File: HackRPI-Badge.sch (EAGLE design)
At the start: 24 parts, among them IC1 74595, IC2 74595, IC3 74595

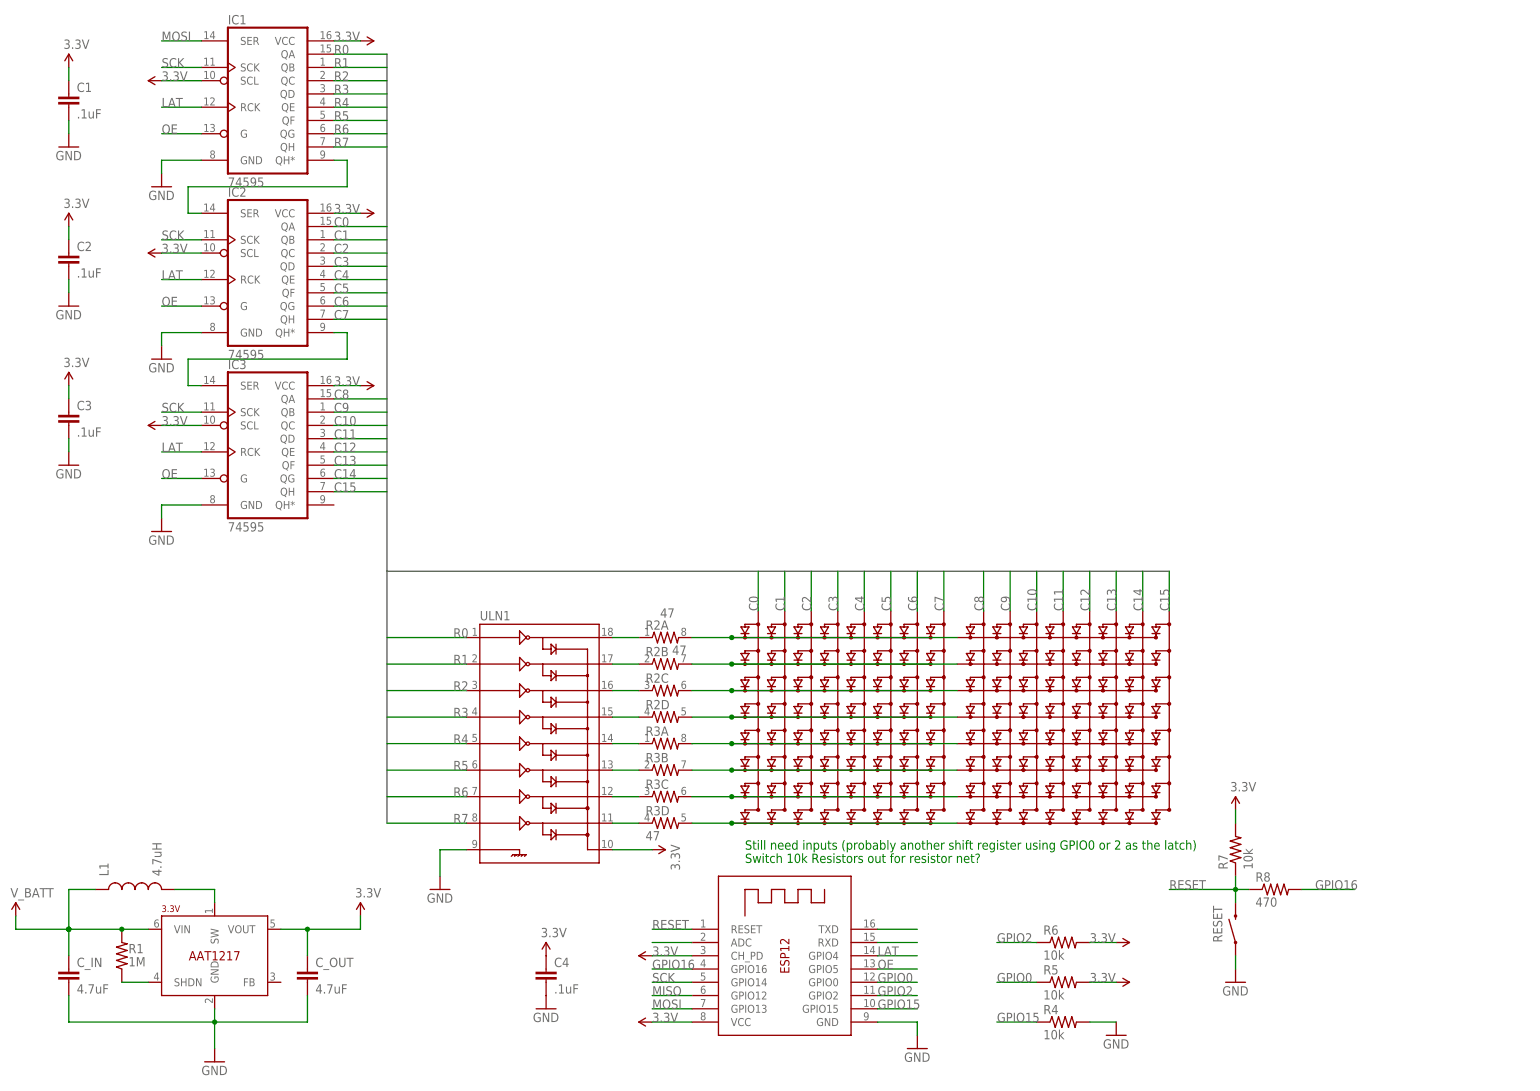
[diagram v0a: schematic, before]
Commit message: Moved resistor nets to ensure constant LED brightness, added serial connector, added 74HC165 for input
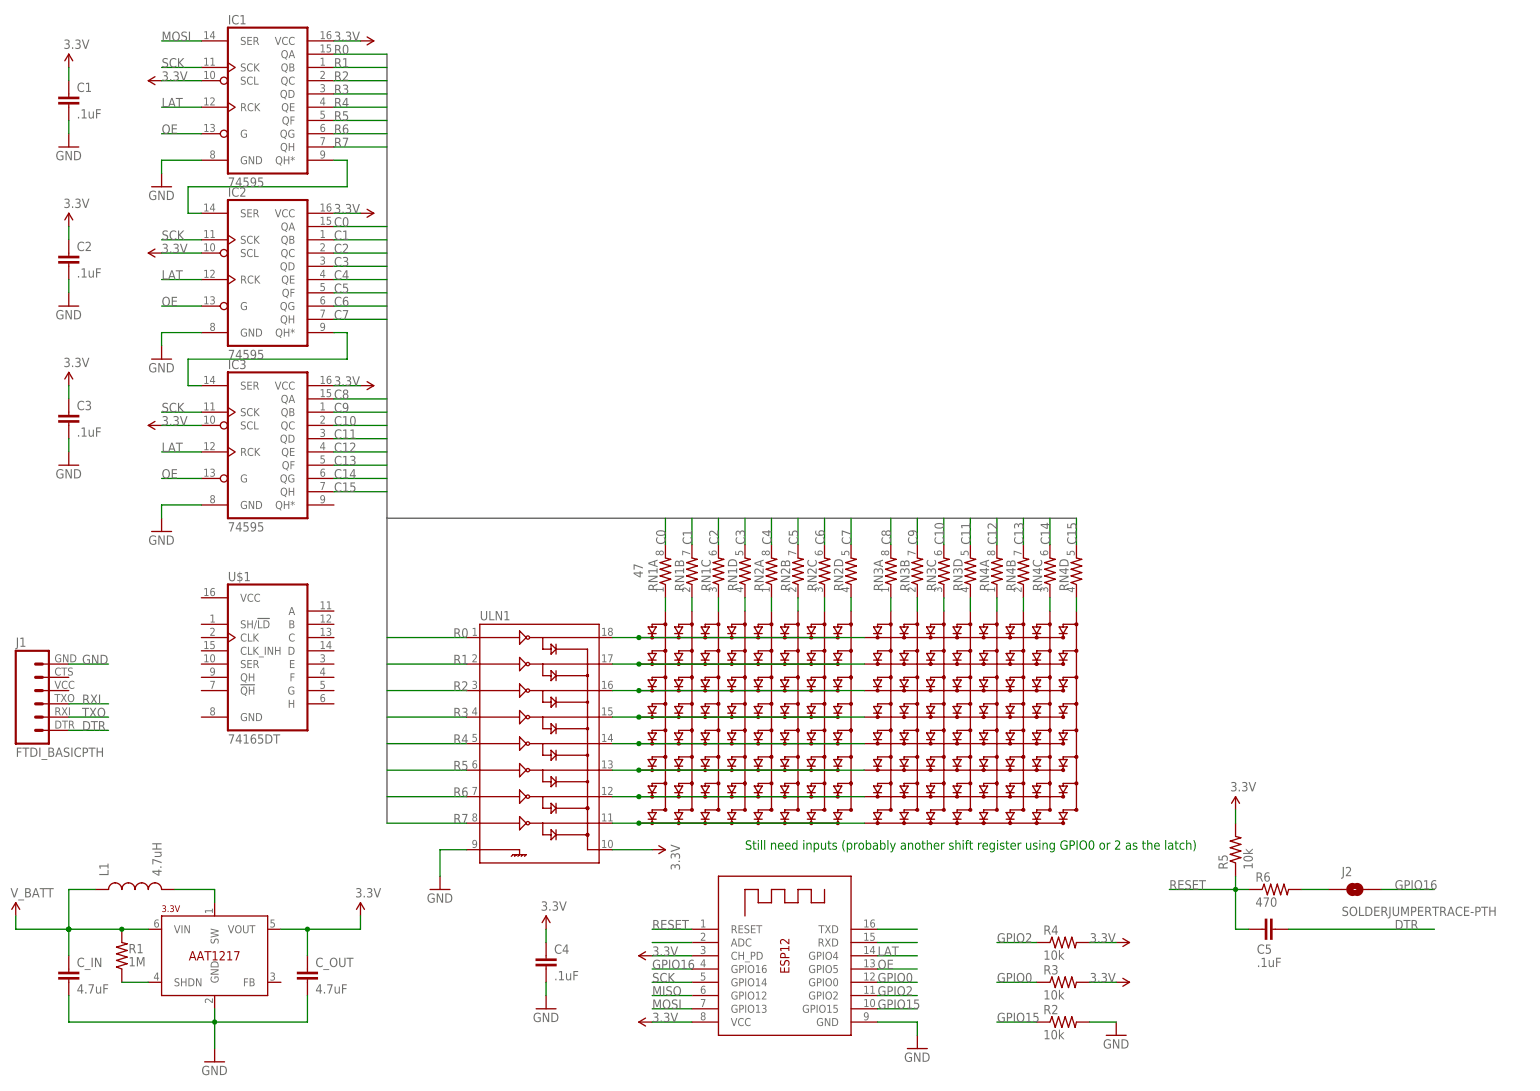
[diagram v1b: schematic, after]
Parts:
- removed R7: 10k, SparkFun-Resistors:RESISTOR0603
- removed R8: 470, SparkFun-Resistors:RESISTOR0603
- removed RESET: SWITCH-MOMENTARY-2SMD, SparkFun-Electromechanical:SWITCH-MOMENTARY-2SMD
- added C5: .1uF, SparkFun-Capacitors:CAP0603-CAP
- added J1: FTDI_BASICPTH, SparkFun-Connectors:FTDI_BASICPTH
- added J2: SOLDERJUMPERTRACE-PTH, SparkFun-Retired:SOLDERJUMPERTRACE-PTH
- added RN1, RN2, RN3, RN4: 47, SparkFun-Passives:RESISTOR-ARRAY0603-ARV
- added U$1: 74165DT, mylib:74165DT
- R2, R3: value 47 -> 10k; device SparkFun-Passives:RESISTOR-ARRAY0603-ARV -> SparkFun-Resistors:RESISTOR0603
- R6: value 10k -> 470
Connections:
- new net DTR: C5.2, J1.1
- new net N$1: J2.1, R6.2
- new net N$10: LED_LEFT.C5, RN2A.1
- new net N$11: LED_LEFT.C6, RN2B.1
- new net N$3: LED_LEFT.C1, RN1A.1
- new net N$4: LED_LEFT.C2, RN1B.1
- new net N$8: LED_LEFT.C3, RN1C.1
- new net N$9: LED_LEFT.C4, RN1D.1
- new net RXI: J1.3, WIFI.RXD
- new net TXO: J1.2, WIFI.TXD
- net 3.3V: now also R3.2, R4.2; no longer R6.2, R7.2
- net C0: now also RN1A.2; no longer LED_LEFT.C1
- net C1: now also RN1B.2; no longer LED_LEFT.C2
- net C10: now also RN3C.2; no longer LEF_RIGHT.C3
- net C11: now also RN3D.2; no longer LEF_RIGHT.C4
- net C12: now also RN4A.2; no longer LEF_RIGHT.C5
- net C13: now also RN4B.2; no longer LEF_RIGHT.C6
- net C14: now also RN4C.2; no longer LEF_RIGHT.C7
- net C15: now also RN4D.2; no longer LEF_RIGHT.C8
- net C2: now also RN1C.2; no longer LED_LEFT.C3
- net C3: now also RN1D.2; no longer LED_LEFT.C4
- net C4: now also RN2A.2; no longer LED_LEFT.C5
- net C5: now also RN2B.2; no longer LED_LEFT.C6
- net C6: now also RN2C.2; no longer LED_LEFT.C7
- net C7: now also RN2D.2; no longer LED_LEFT.C8
- net C8: now also RN3A.2; no longer LEF_RIGHT.C1
- net C9: now also RN3B.2; no longer LEF_RIGHT.C2
- net GND: now also J1.6, R2.2; no longer R4.2, RESET.1
- net GPIO0: now also R3.1; no longer R5.1
- net GPIO15: now also R2.1; no longer R4.1
- net GPIO16: now also J2.2; no longer R8.2
- net GPIO2: now also R4.1; no longer R6.1
- net N$12: now also LED_LEFT.C7, RN2C.1; no longer WIFI.RXD
- net N$13: now also LED_LEFT.C8, RN2D.1; no longer WIFI.TXD
- net N$14: now also ULN1.17; no longer R2B.2
- net N$15: now also ULN1.16; no longer R2C.2
- net N$16: now also ULN1.15; no longer R2D.2
- net N$17: now also ULN1.14; no longer R3A.2
- net N$18: now also ULN1.13; no longer R3B.2
- net N$19: now also ULN1.12; no longer R3C.2
- net N$20: now also ULN1.11; no longer R3D.2
- net N$23: now also LEF_RIGHT.C1, RN3A.1; no longer R2A.1, ULN1.18
- net N$24: now also LEF_RIGHT.C2, RN3B.1; no longer R2B.1, ULN1.17
- net N$25: now also LEF_RIGHT.C3, RN3C.1; no longer R2C.1, ULN1.16
- net N$26: now also LEF_RIGHT.C4, RN3D.1; no longer R2D.1, ULN1.15
- net N$27: now also LEF_RIGHT.C5, RN4A.1; no longer R3A.1, ULN1.14
- net N$28: now also LEF_RIGHT.C6, RN4B.1; no longer R3B.1, ULN1.13
- net N$29: now also LEF_RIGHT.C7, RN4C.1; no longer R3C.1, ULN1.12
- net N$30: now also LEF_RIGHT.C8, RN4D.1; no longer R3D.1, ULN1.11
- net N$7: now also ULN1.18; no longer R2A.2
- net RESET: now also C5.1, R5.1, R6.1; no longer R7.1, R8.1, RESET.2
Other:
- note removed: "Switch 10k Resistors out for resistor net?"
- moved on the sheet: C4, R4, R5, R6

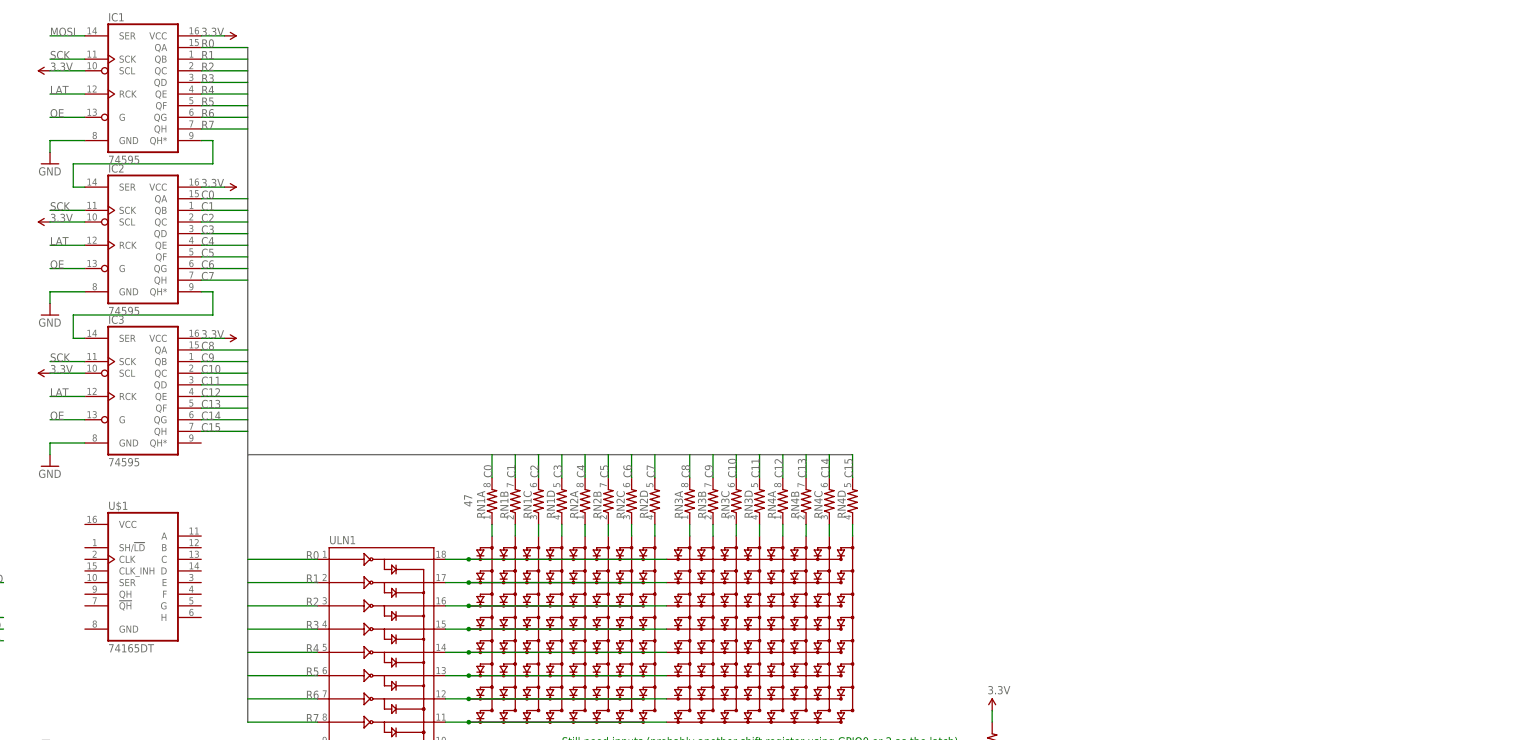
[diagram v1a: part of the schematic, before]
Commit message: Updated part names, misc work
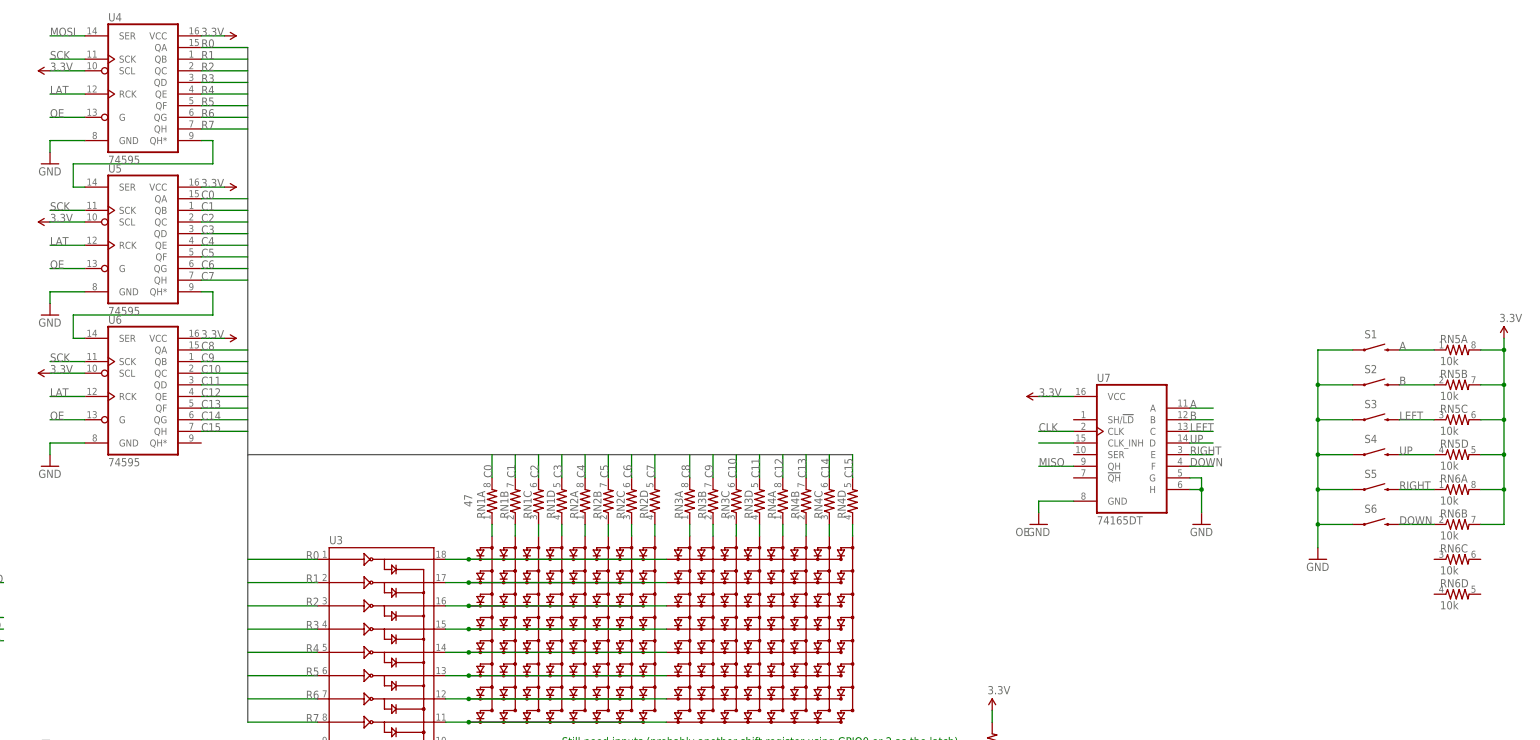
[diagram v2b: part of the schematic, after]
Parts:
- removed U$1: 74165DT, mylib:74165DT
- added RN5, RN6: 10k, SparkFun-Passives:RESISTOR-ARRAY0603-ARV
- added S1, S2, S3, S4, S5, S6: SWITCH-MOMENTARY-2PTH, SparkFun-Electromechanical:SWITCH-MOMENTARY-2PTH
- added U7: 74165DT, mylib:74165DT
- renumbered IC1 to U4, IC2 to U5, IC3 to U6, REG to U2, ULN1 to U3, WIFI to U1
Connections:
- new net A: RN5A.1, S1.2, U7.A
- new net B: RN5B.1, S2.2, U7.B
- new net CLK: U7.CLK
- new net DOWN: RN6B.1, S6.2, U7.F
- new net LEFT: RN5C.1, S3.2, U7.C
- new net RIGHT: RN6A.1, S5.2, U7.E
- new net UP: RN5D.1, S4.2, U7.D
- net 3.3V: now also RN5A.2, RN5B.2, RN5C.2, RN5D.2, RN6A.2, RN6B.2, U7.VCC
- net GND: now also S1.1, S2.1, S3.1, S4.1, S5.1, S6.1, U7.G, U7.GND, U7.H
- net MISO: now also U7.QH
- net OE: now also U7.CLK_INH

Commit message: Placed components on board, routed LED matrices and output shift registers, rounded corners of board
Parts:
- added BAT1, BAT2: (no value), SparkFun-Electromechanical:BATTERYAAA
- added C6, C7: .1uF, SparkFun-Capacitors:CAP0603-CAP
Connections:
- new net N$31: BAT1.-, BAT2.+
- net 3.3V: now also C6.1, C7.1, RN5A.1, RN5B.1, RN5C.1, RN5D.1, RN6A.1, RN6B.1, RN6C.1, RN6D.1; no longer RN5A.2, RN5B.2, RN5C.2, RN5D.2, RN6A.2, RN6B.2
- net A: now also RN6A.2, S5.2, U7.E; no longer RN5A.1, S1.2, U7.A
- net B: now also RN6B.2, S6.2, U7.F; no longer RN5B.1, S2.2, U7.B
- net DOWN: now also RN5A.2, S4.2, U7.D; no longer RN6B.1, S6.2, U7.F
- net GND: now also BAT2.-, C6.2, C7.2
- net GPIO0: now also U7.SH/!LD
- net GPIO2: now also U7.CLK_INH
- net LEFT: now also RN5D.2, S1.2, U7.A; no longer RN5C.1, S3.2, U7.C
- net OE: no longer U7.CLK_INH
- net R0: now also U3.8; no longer U3.1
- net R1: now also U3.7; no longer U3.2
- net R2: now also U3.6; no longer U3.3
- net R3: now also U3.5; no longer U3.4
- net R4: now also U3.4; no longer U3.5
- net R5: now also U3.3; no longer U3.6
- net R6: now also U3.2; no longer U3.7
- net R7: now also U3.1; no longer U3.8
- net RIGHT: now also RN5B.2, S3.2, U7.C; no longer RN6A.1, S5.2, U7.E
- net UP: now also RN5C.2, S2.2, U7.B; no longer RN5D.1, S4.2, U7.D
- net V_BATT: now also BAT1.+
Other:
- moved on the sheet: RN5A, RN5B, RN5C, RN5D, RN6A, RN6B, RN6C, RN6D, S1, S2, S3, S4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

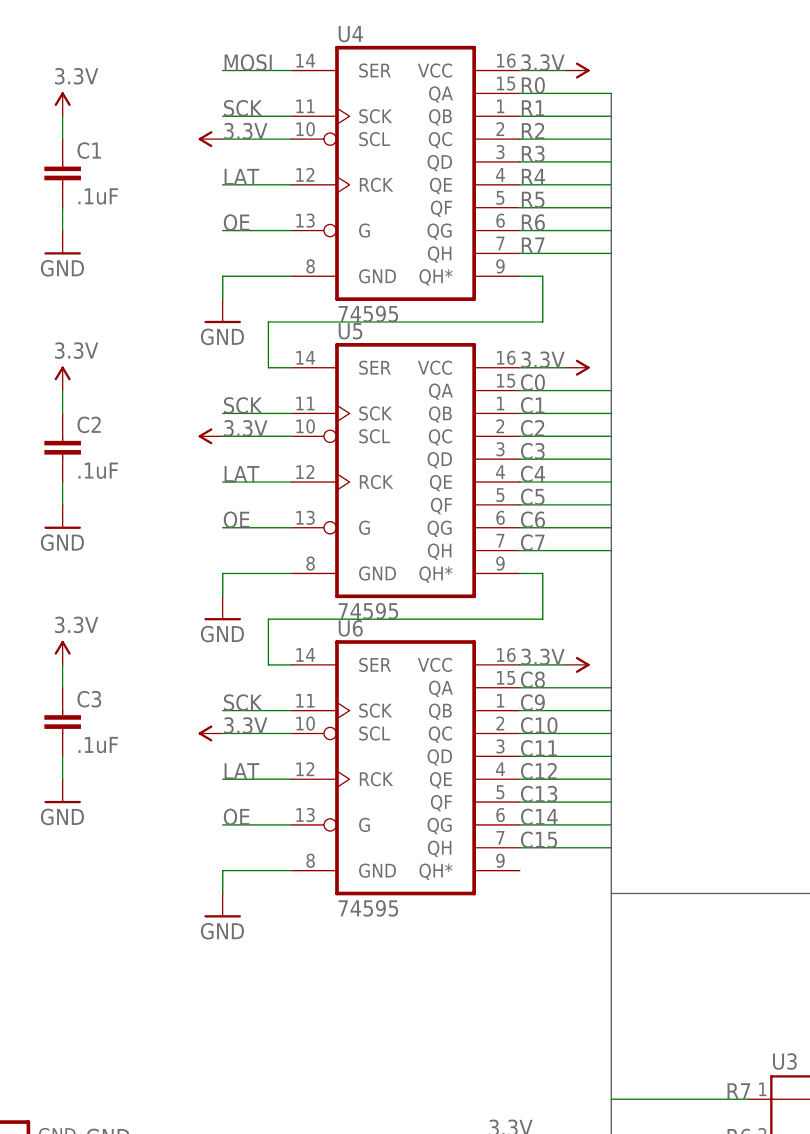
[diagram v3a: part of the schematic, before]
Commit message: Finished laying out/routing first revision of board
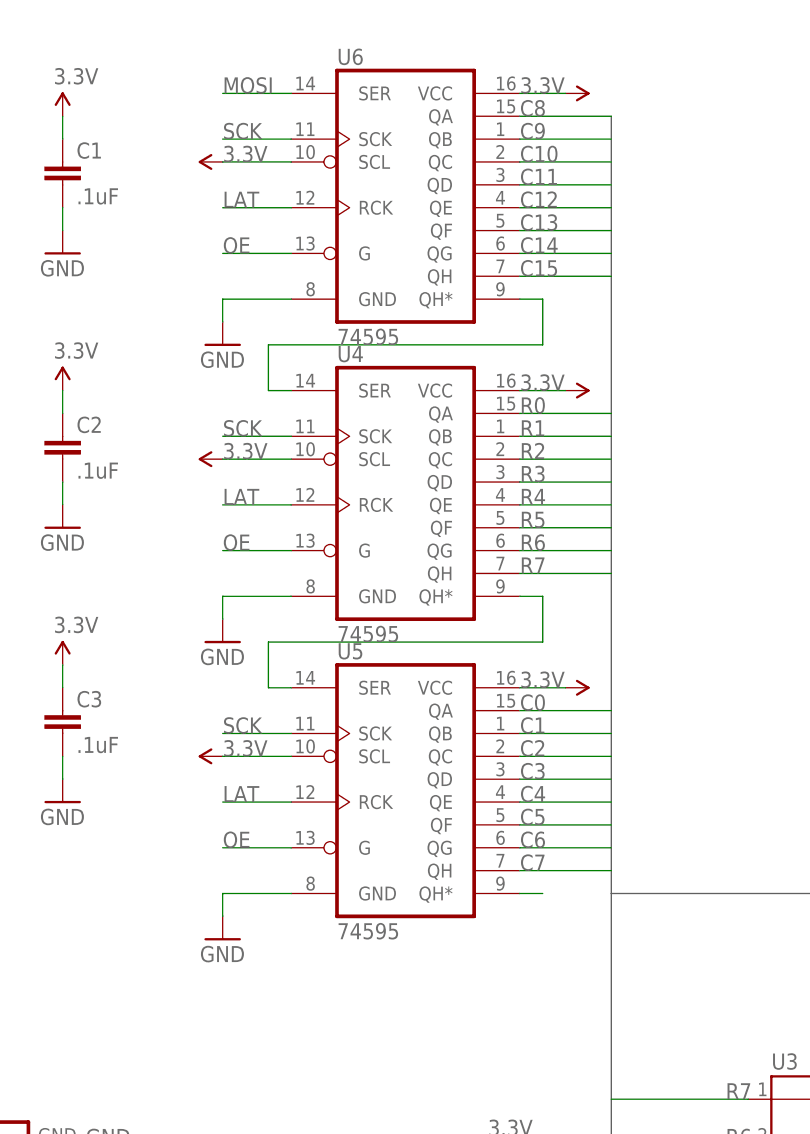
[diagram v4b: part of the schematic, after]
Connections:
- new net N$33: U5.QH*
- net MOSI: now also U6.SER; no longer U4.SER
- net N$22: now also U4.SER, U6.QH*; no longer U5.QH*, U6.SER
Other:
- moved on the sheet: U4, U5, U6
